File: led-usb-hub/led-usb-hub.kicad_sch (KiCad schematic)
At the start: 29 parts, among them J1 USB_C_Receptacle_USB2.0, J2 USB_A_RGB, J3 USB_A_RGB, J4 USB_A_RGB, SW1 SW_Push, U1 SL2.1A, U2 KB2040, Y1 12MHz

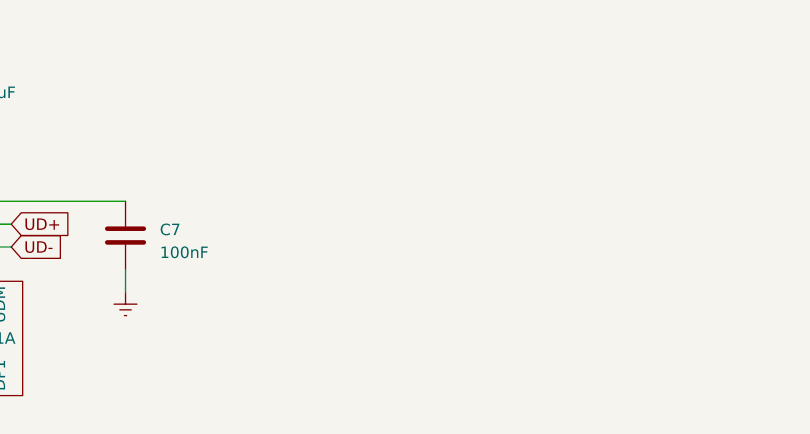
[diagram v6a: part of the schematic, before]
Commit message: Add holes and graphics Tune trace length
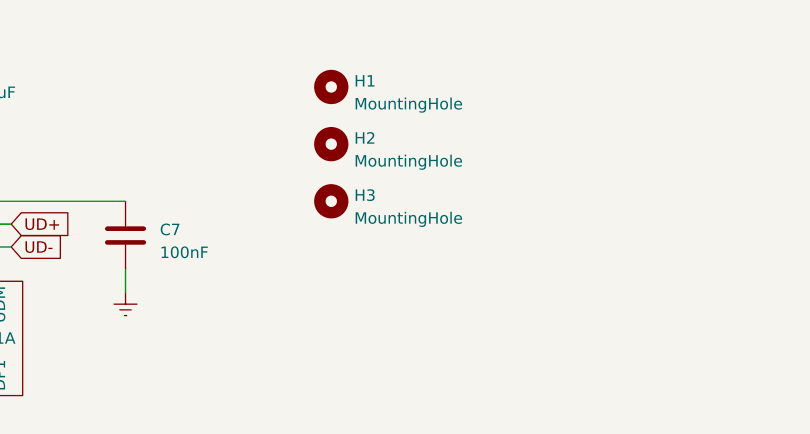
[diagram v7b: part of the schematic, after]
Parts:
- added H1, H2, H3: MountingHole, MountingHole:MountingHole_3.2mm_M3, symbol Mechanical:MountingHole
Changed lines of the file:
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@@
+    )
+  )
+  (symbol (lib_id "Mechanical:MountingHole") (at 214.63 30.48 0) (unit 1)
+    (in_bom yes) (on_board yes) (dnp no) (fields_autoplaced)
+    (property "Reference" "H2" (at 217.17 29.845 0)
+      (effects (font (size 1.27 1.27)) (justify left))
+    )
+    (property "Value" "MountingHole" (at 217.17 32.385 0)
+      (effects (font (size 1.27 1.27)) (justify left))
+    )
+    (property "Footprint" "MountingHole:MountingHole_3.2mm_M3" (at 214.63 30.48 0)
+      (effects (font (size 1.27 1.27)) hide)
+    )
+    (property "Datasheet" "~" (at 214.63 30.48 0)
+      (effects (font (size 1.27 1.27)) hide)
+    )
+    (instances
+      (project "led-usb-hub"
+        (path "/872229b5-49ea-4e15-b82a-ed1f213c1d75"
+          (reference "H2") (unit 1)
+        )
+      )
     )
   )
@@
     )
     (pin "1")
+    (pin "2")
     (pin "3")
-    (pin "2")
     (pin "4")
     (instances
@@
     )
   )
+  (symbol (lib_id "Mechanical:MountingHole") (at 214.63 36.83 0) (unit 1)
+    (in_bom yes) (on_board yes) (dnp no) (fields_autoplaced)
+    (property "Reference" "H3" (at 217.17 36.195 0)
+      (effects (font (size 1.27 1.27)) (justify left))
+    )
+    (property "Value" "MountingHole" (at 217.17 38.735 0)
+      (effects (font (size 1.27 1.27)) (justify left))
+    )
+    (property "Footprint" "MountingHole:MountingHole_3.2mm_M3" (at 214.63 36.83 0)
+      (effects (font (size 1.27 1.27)) hide)
+    )
+    (property "Datasheet" "~" (at 214.63 36.83 0)
+      (effects (font (size 1.27 1.27)) hide)
+    )
+    (instances
+      (project "led-usb-hub"
+        (path "/872229b5-49ea-4e15-b82a-ed1f213c1d75"
+          (reference "H3") (unit 1)
+        )
+      )
+    )
+  )
   (symbol (lib_id "Device:R_US") (at 135.89 113.03 0) (unit 1)
     (in_bom yes) (on_board yes) (dnp no) (fields_autoplaced)
@@
         )
       )
+    )
+  )
+  (symbol (lib_id "Mechanical:MountingHole") (at 214.63 24.13 0) (unit 1)
+    (in_bom yes) (on_board yes) (dnp no) (fields_autoplaced)
+    (property "Reference" "H1" (at 217.17 23.495 0)
+      (effects (font (size 1.27 1.27)) (justify left))
+    )
+    (property "Value" "MountingHole" (at 217.17 26.035 0)
+      (effects (font (size 1.27 1.27)) (justify left))
+    )
+    (property "Footprint" "MountingHole:MountingHole_3.2mm_M3" (at 214.63 24.13 0)
+      (effects (font (size 1.27 1.27)) hide)
+    )
+    (property "Datasheet" "~" (at 214.63 24.13 0)
+      (effects (font (size 1.27 1.27)) hide)
+    )
+    (instances
+      (project "led-usb-hub"
+        (path "/872229b5-49ea-4e15-b82a-ed1f213c1d75"
+          (reference "H1") (unit 1)
+        )
+      )

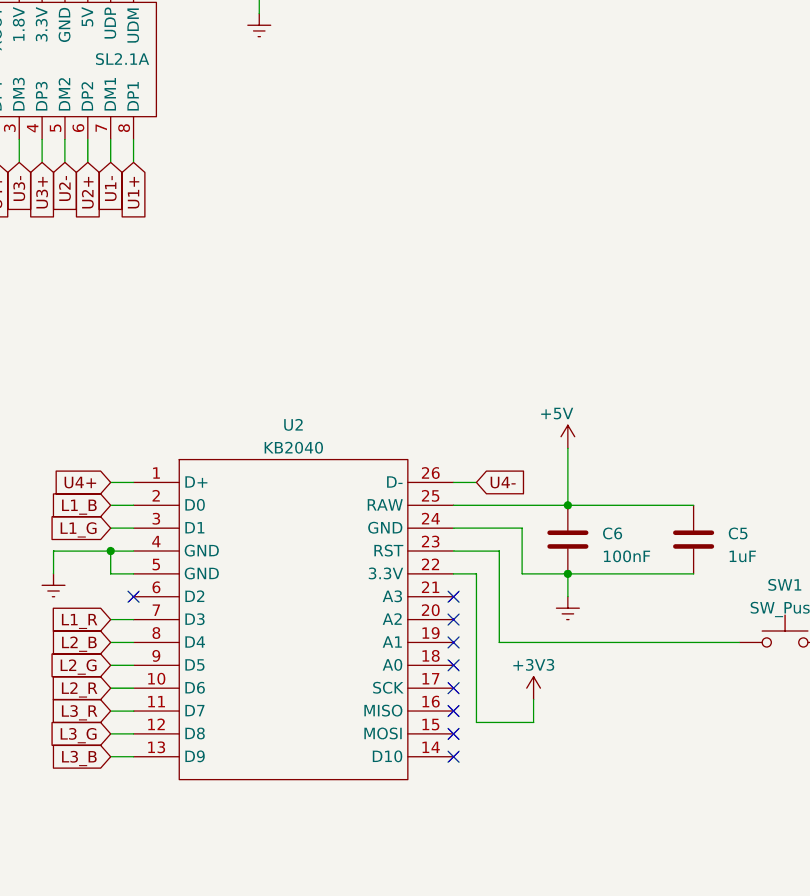
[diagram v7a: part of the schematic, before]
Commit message: Add indicator LEDs
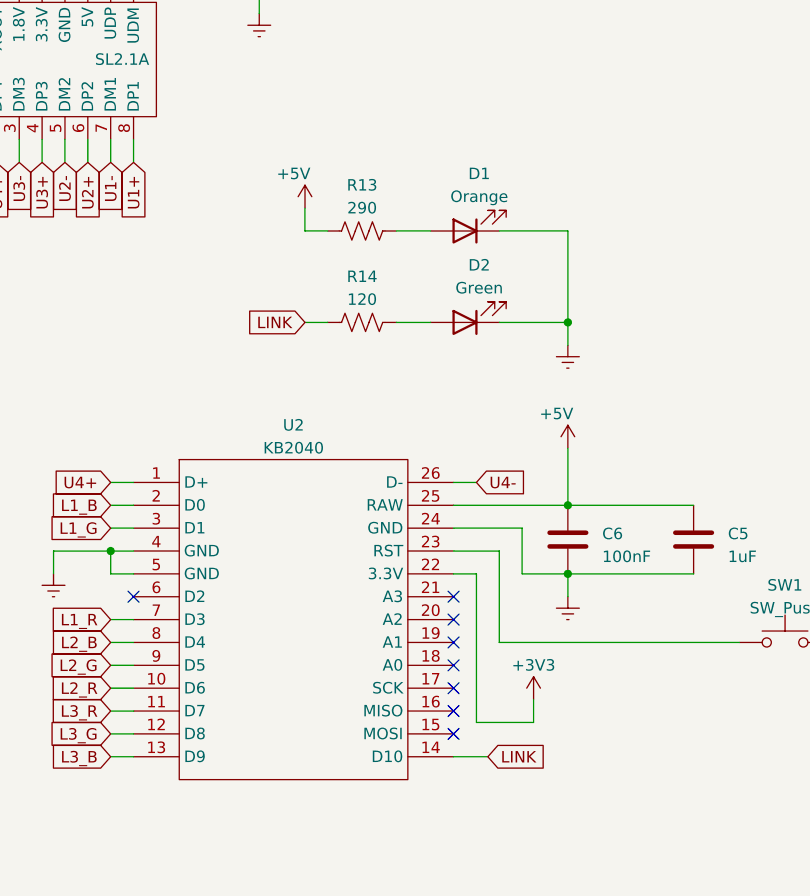
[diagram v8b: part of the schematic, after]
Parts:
- added D1: Orange, LED_SMD:LED-APA2106C, symbol Device:LED
- added D2: Green, LED_SMD:LED-APA2106C, symbol Device:LED
- added R13: 290, Resistor_SMD:R_0603_1608Metric_Pad0.98x0.95mm_HandSolder, symbol Device:R_US
- added R14: 120, Resistor_SMD:R_0603_1608Metric_Pad0.98x0.95mm_HandSolder, symbol Device:R_US
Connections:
- net +5V: now also R13.1
- net Earth: now also D1.1 (K), D2.1 (K)
- net LINK: now reaches U2.14 (D10)
- net LINK: now also R14.1
- new net: D1.2 (A), R13.2
- new net: D2.2 (A), R14.2
- no-connect marks 11 -> 10
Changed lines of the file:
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@@
   (junction (at 175.26 106.68) (diameter 0) (color 0 0 0 0)
+  )
+  (junction (at 226.06 81.28) (diameter 0) (color 0 0 0 0)
   )
   (junction (at 151.13 40.64) (diameter 0) (color 0 0 0 0)
@@
   (no_connect (at 67.31 54.61))
   (no_connect (at 67.31 52.07))
-  (no_connect (at 213.36 129.54))
   (no_connect (at 213.36 121.92))
   (no_connect (at 177.8 111.76))
@@
     (stroke (width 0) (type default))
   )
+  (wire (pts (xy 226.06 81.28) (xy 226.06 83.82))
+    (stroke (width 0) (type default))
+  )
   (wire (pts (xy 114.3 115.57) (xy 114.3 113.03))
     (stroke (width 0) (type default))
@@
     (stroke (width 0) (type default))
   )
+  (wire (pts (xy 196.85 81.28) (xy 199.39 81.28))
+    (stroke (width 0) (type default))
+  )
   (wire (pts (xy 179.07 39.37) (xy 175.26 39.37))
     (stroke (width 0) (type default))
@@
     (stroke (width 0) (type default))
   )
+  (wire (pts (xy 207.01 81.28) (xy 210.82 81.28))
+    (stroke (width 0) (type default))
+  )
   (wire (pts (xy 226.06 101.6) (xy 240.03 101.6))
     (stroke (width 0) (type default))
@@
     (stroke (width 0) (type default))
   )
+  (wire (pts (xy 226.06 71.12) (xy 218.44 71.12))
+    (stroke (width 0) (type default))
+  )
   (wire (pts (xy 260.35 116.84) (xy 260.35 119.38))
     (stroke (width 0) (type default))
@@
     (stroke (width 0) (type default))
   )
+  (wire (pts (xy 207.01 71.12) (xy 210.82 71.12))
+    (stroke (width 0) (type default))
+  )
   (wire (pts (xy 161.29 17.78) (xy 165.1 17.78))
     (stroke (width 0) (type default))
@@
     (stroke (width 0) (type default))
   )
+  (wire (pts (xy 218.44 81.28) (xy 226.06 81.28))
+    (stroke (width 0) (type default))
+  )
   (wire (pts (xy 222.25 125.73) (xy 215.9 125.73))
     (stroke (width 0) (type default))
@@
     (stroke (width 0) (type default))
   )
+  (wire (pts (xy 226.06 81.28) (xy 226.06 71.12))
+    (stroke (width 0) (type default))
+  )
   (wire (pts (xy 160.02 40.64) (xy 160.02 43.18))
     (stroke (width 0) (type default))
@@
     (stroke (width 0) (type default))
   )
+  (wire (pts (xy 196.85 71.12) (xy 199.39 71.12))
+    (stroke (width 0) (type default))
+  )
   (wire (pts (xy 43.18 124.46) (xy 43.18 134.62))
     (stroke (width 0) (type default))
@@
     (stroke (width 0) (type default))
   )
+  (wire (pts (xy 196.85 68.58) (xy 196.85 71.12))
+    (stroke (width 0) (type default))
+  )
   (wire (pts (xy 167.64 17.78) (xy 167.64 43.18))
+    (stroke (width 0) (type default))
+  )
+  (wire (pts (xy 213.36 129.54) (xy 217.17 129.54))
     (stroke (width 0) (type default))
   )
@@
     )
   )
+  (global_label "LINK" (shape input) (at 217.17 129.54 0) (fields_autoplaced)
+    (effects (font (size 1.27 1.27)) (justify left))
+    (property "Intersheetrefs" "${INTERSHEET_REFS}" (at 224.3092 129.54 0)
+      (effects (font (size 1.27 1.27)) (justify left) hide)
+    )
+  )
   (global_label "U1+" (shape input) (at 177.8 63.5 270) (fields_autoplaced)
     (effects (font (size 1.27 1.27)) (justify right))
@@
     )
   )
+  (global_label "LINK" (shape input) (at 196.85 81.28 180) (fields_autoplaced)
+    (effects (font (size 1.27 1.27)) (justify right))
+    (property "Intersheetrefs" "${INTERSHEET_REFS}" (at 189.7108 81.28 0)
+      (effects (font (size 1.27 1.27)) (justify right) hide)
+    )
+  )
   (global_label "L2_B" (shape input) (at 80.01 134.62 270) (fields_autoplaced)
     (effects (font (size 1.27 1.27)) (justify right))
@@
         (path "/872229b5-49ea-4e15-b82a-ed1f213c1d75"
           (reference "#PWR025") (unit 1)
+        )
+      )
+    )
+  )
+  (symbol (lib_id "power:Earth") (at 226.06 83.82 0) (unit 1)
+    (in_bom yes) (on_board yes) (dnp no) (fields_autoplaced)
+    (property "Reference" "#PWR023" (at 226.06 90.17 0)
+      (effects (font (size 1.27 1.27)) hide)
+    )
+    (property "Value" "Earth" (at 226.06 87.63 0)
+      (effects (font (size 1.27 1.27)) hide)
+    )
+    (property "Footprint" "" (at 226.06 83.82 0)
+      (effects (font (size 1.27 1.27)) hide)
+    )
+    (property "Datasheet" "~" (at 226.06 83.82 0)
+      (effects (font (size 1.27 1.27)) hide)
+    )
+    (pin "1")
+    (instances
+      (project "led-usb-hub"
+        (path "/872229b5-49ea-4e15-b82a-ed1f213c1d75"
+          (reference "#PWR023") (unit 1)
         )
       )
@@
     )
   )
+  (symbol (lib_id "Device:R_US") (at 203.2 71.12 90) (unit 1)
+    (in_bom yes) (on_board yes) (dnp no) (fields_autoplaced)
+    (property "Reference" "R13" (at 203.2 66.04 90)
+      (effects (font (size 1.27 1.27)))
+    )
+    (property "Value" "290" (at 203.2 68.58 90)
+      (effects (font (size 1.27 1.27)))
+    )
+    (property "Footprint" "Resistor_SMD:R_0603_1608Metric_Pad0.98x0.95mm_HandSolder" (at 203.454 70.104 90)
+      (effects (font (size 1.27 1.27)) hide)
+    )
+    (property "Datasheet" "~" (at 203.2 71.12 0)
+      (effects (font (size 1.27 1.27)) hide)
+    )
+    (pin "1")
+    (pin "2")
+    (instances
+      (project "led-usb-hub"
+        (path "/872229b5-49ea-4e15-b82a-ed1f213c1d75"
+          (reference "R13") (unit 1)
+        )
+      )
+    )
+  )
   (symbol (lib_id "Device:R_US") (at 81.28 38.1 180) (unit 1)
     (in_bom yes) (on_board yes) (dnp no) (fields_autoplaced)
@@
     )
   )
+  (symbol (lib_id "Device:LED") (at 214.63 71.12 180) (unit 1)
+    (in_bom yes) (on_board yes) (dnp no) (fields_autoplaced)
+    (property "Reference" "D1" (at 216.2175 64.77 0)
+      (effects (font (size 1.27 1.27)))
+    )
+    (property "Value" "Orange" (at 216.2175 67.31 0)
+      (effects (font (size 1.27 1.27)))
+    )
+    (property "Footprint" "LED_SMD:LED-APA2106C" (at 214.63 71.12 0)
+      (effects (font (size 1.27 1.27)) hide)
+    )
+    (property "Datasheet" "~" (at 214.63 71.12 0)
+      (effects (font (size 1.27 1.27)) hide)
+    )
+    (pin "1")
+    (pin "2")
+    (instances
+      (project "led-usb-hub"
+        (path "/872229b5-49ea-4e15-b82a-ed1f213c1d75"
+          (reference "D1") (unit 1)
+        )
+      )
+    )
+  )
   (symbol (lib_id "Device:C") (at 100.33 38.1 0) (unit 1)
     (in_bom yes) (on_board yes) (dnp no) (fields_autoplaced)
@@
     )
   )
+  (symbol (lib_id "power:+5V") (at 196.85 68.58 0) (unit 1)
+    (in_bom yes) (on_board yes) (dnp no)
+    (property "Reference" "#PWR024" (at 196.85 72.39 0)
+      (effects (font (size 1.27 1.27)) hide)
+    )
+    (property "Value" "+5V" (at 195.58 64.77 0)
+      (effects (font (size 1.27 1.27)))
+    )
+    (property "Footprint" "" (at 196.85 68.58 0)
+      (effects (font (size 1.27 1.27)) hide)
+    )
+    (property "Datasheet" "" (at 196.85 68.58 0)
+      (effects (font (size 1.27 1.27)) hide)
+    )
+    (pin "1")
+    (instances
+      (project "led-usb-hub"
+        (path "/872229b5-49ea-4e15-b82a-ed1f213c1d75"
+          (reference "#PWR024") (unit 1)
+        )
+      )
+    )
+  )
   (symbol (lib_id "Device:R_US") (at 123.19 128.27 0) (unit 1)
     (in_bom yes) (on_board yes) (dnp no) (fields_autoplaced)
@@
         (path "/872229b5-49ea-4e15-b82a-ed1f213c1d75"
           (reference "R11") (unit 1)
+        )
+      )
+    )
+  )
+  (symbol (lib_id "Device:LED") (at 214.63 81.28 180) (unit 1)
+    (in_bom yes) (on_board yes) (dnp no) (fields_autoplaced)
+    (property "Reference" "D2" (at 216.2175 74.93 0)
+      (effects (font (size 1.27 1.27)))
+    )
+    (property "Value" "Green" (at 216.2175 77.47 0)
+      (effects (font (size 1.27 1.27)))
+    )
+    (property "Footprint" "LED_SMD:LED-APA2106C" (at 214.63 81.28 0)
+      (effects (font (size 1.27 1.27)) hide)
+    )
+    (property "Datasheet" "~" (at 214.63 81.28 0)
+      (effects (font (size 1.27 1.27)) hide)
+    )
+    (pin "1")
+    (pin "2")
+    (instances
+      (project "led-usb-hub"
+        (path "/872229b5-49ea-4e15-b82a-ed1f213c1d75"
+          (reference "D2") (unit 1)
         )
       )
@@
         )
       )
+    )
+  )
+  (symbol (lib_id "Device:R_US") (at 203.2 81.28 90) (unit 1)
+    (in_bom yes) (on_board yes) (dnp no) (fields_autoplaced)
+    (property "Reference" "R14" (at 203.2 76.2 90)
+      (effects (font (size 1.27 1.27)))
+    )
+    (property "Value" "120" (at 203.2 78.74 90)
+      (effects (font (size 1.27 1.27)))
+    )
+    (property "Footprint" "Resistor_SMD:R_0603_1608Metric_Pad0.98x0.95mm_HandSolder" (at 203.454 80.264 90)
+      (effects (font (size 1.27 1.27)) hide)
+    )
+    (property "Datasheet" "~" (at 203.2 81.28 0)
+      (effects (font (size 1.27 1.27)) hide)
+    )
+    (pin "1")
+    (pin "2")
+    (instances
+      (project "led-usb-hub"
+        (path "/872229b5-49ea-4e15-b82a-ed1f213c1d75"
+          (reference "R14") (unit 1)
+        )
+      )
